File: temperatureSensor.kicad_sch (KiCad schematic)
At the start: 3 parts, among them J2 Conn_01x03_Pin

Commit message: revision
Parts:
- added TP1: TestPoint, TestPoint:TestPoint_THTPad_D2.0mm_Drill1.0mm, symbol Connector:TestPoint
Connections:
- net tempSensor1_OUT: now also TP1.1
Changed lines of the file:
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@@
     (effects (font (size 1.27 1.27)) (justify right))
+  )
+  (symbol (lib_id "Connector:TestPoint") (at 68.58 74.93 0) (unit 1)
+    (in_bom yes) (on_board yes) (dnp no) (fields_autoplaced)
+    (property "Reference" "TP1" (at 71.12 70.358 0)
+      (effects (font (size 1.27 1.27)) (justify left))
+    )
+    (property "Value" "TestPoint" (at 71.12 72.898 0)
+      (effects (font (size 1.27 1.27)) (justify left))
+    )
+    (property "Footprint" "TestPoint:TestPoint_THTPad_D2.0mm_Drill1.0mm" (at 73.66 74.93 0)
+      (effects (font (size 1.27 1.27)) hide)
+    )
+    (property "Datasheet" "~" (at 73.66 74.93 0)
+      (effects (font (size 1.27 1.27)) hide)
+    )
+    (pin "1")
+    (instances
+      (project "Telemetry-Peripheral-SOM-Daughterboard-IMU"
+        (path "/637f68f0-cb9c-412a-8573-5d8e7ef6d8a2/0366cb5e-31c7-40b1-9d0c-97ad688b48f0"
+          (reference "TP1") (unit 1)
+        )
+      )
+    )
   )
   (symbol (lib_id "Device:C") (at 110.49 97.79 0) (unit 1)

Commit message: Integrated changes made by BPS
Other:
- moved on the sheet: C7, C8, J2, TP1

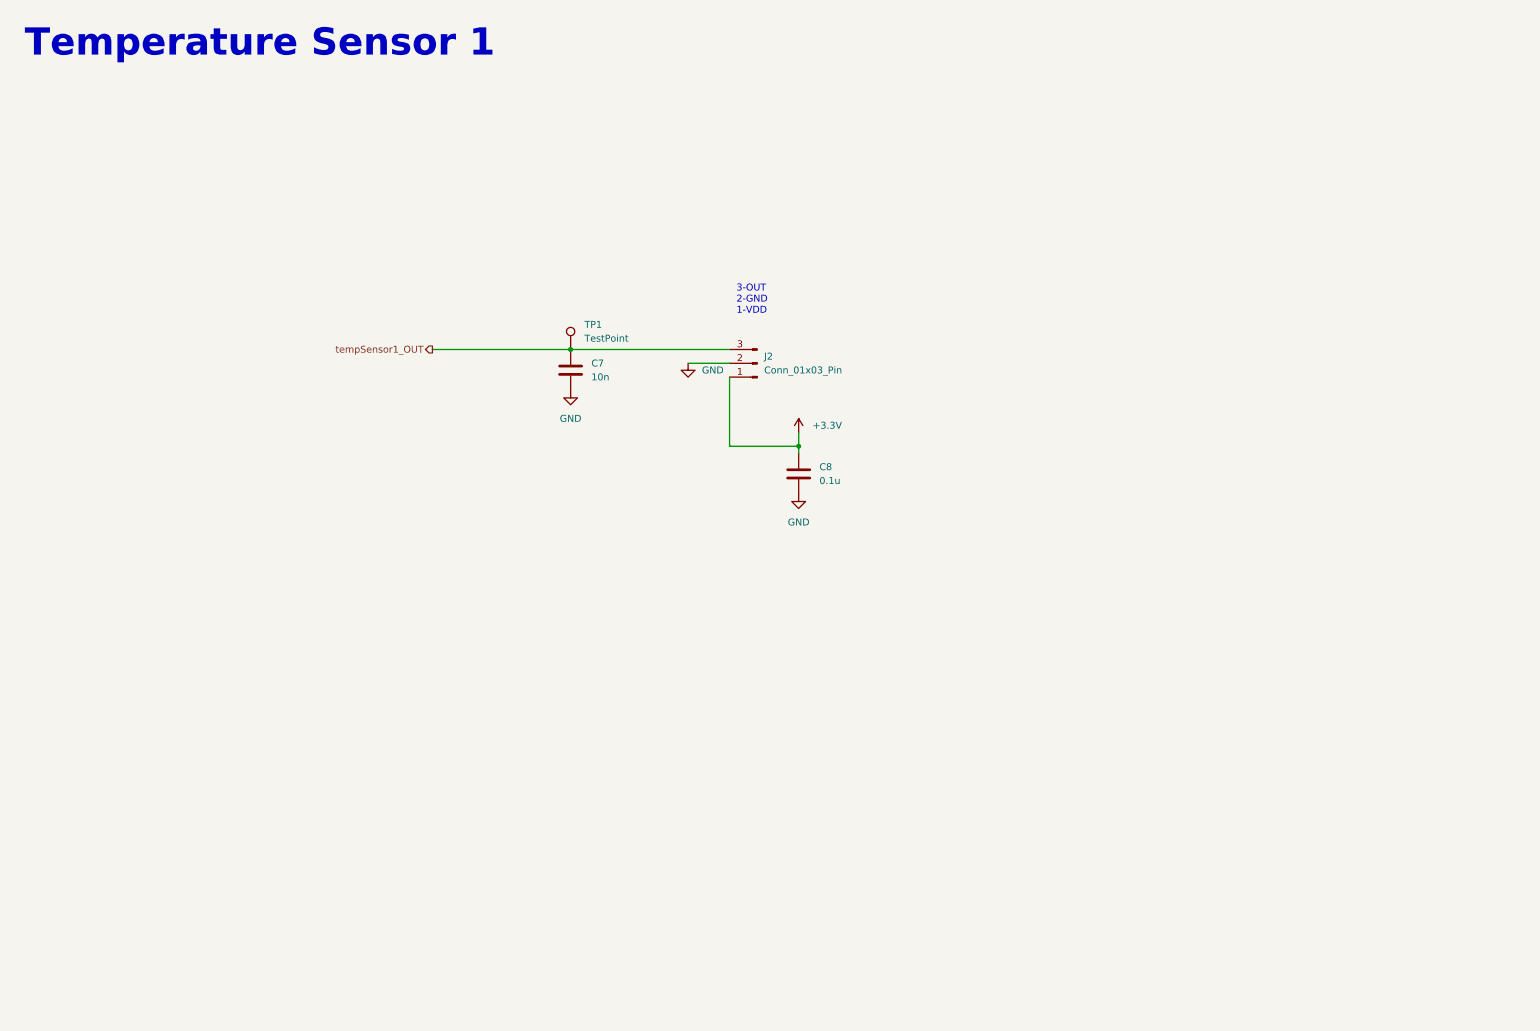
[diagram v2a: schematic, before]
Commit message: added protective circuitry for temp sensors, made name changes for IMU
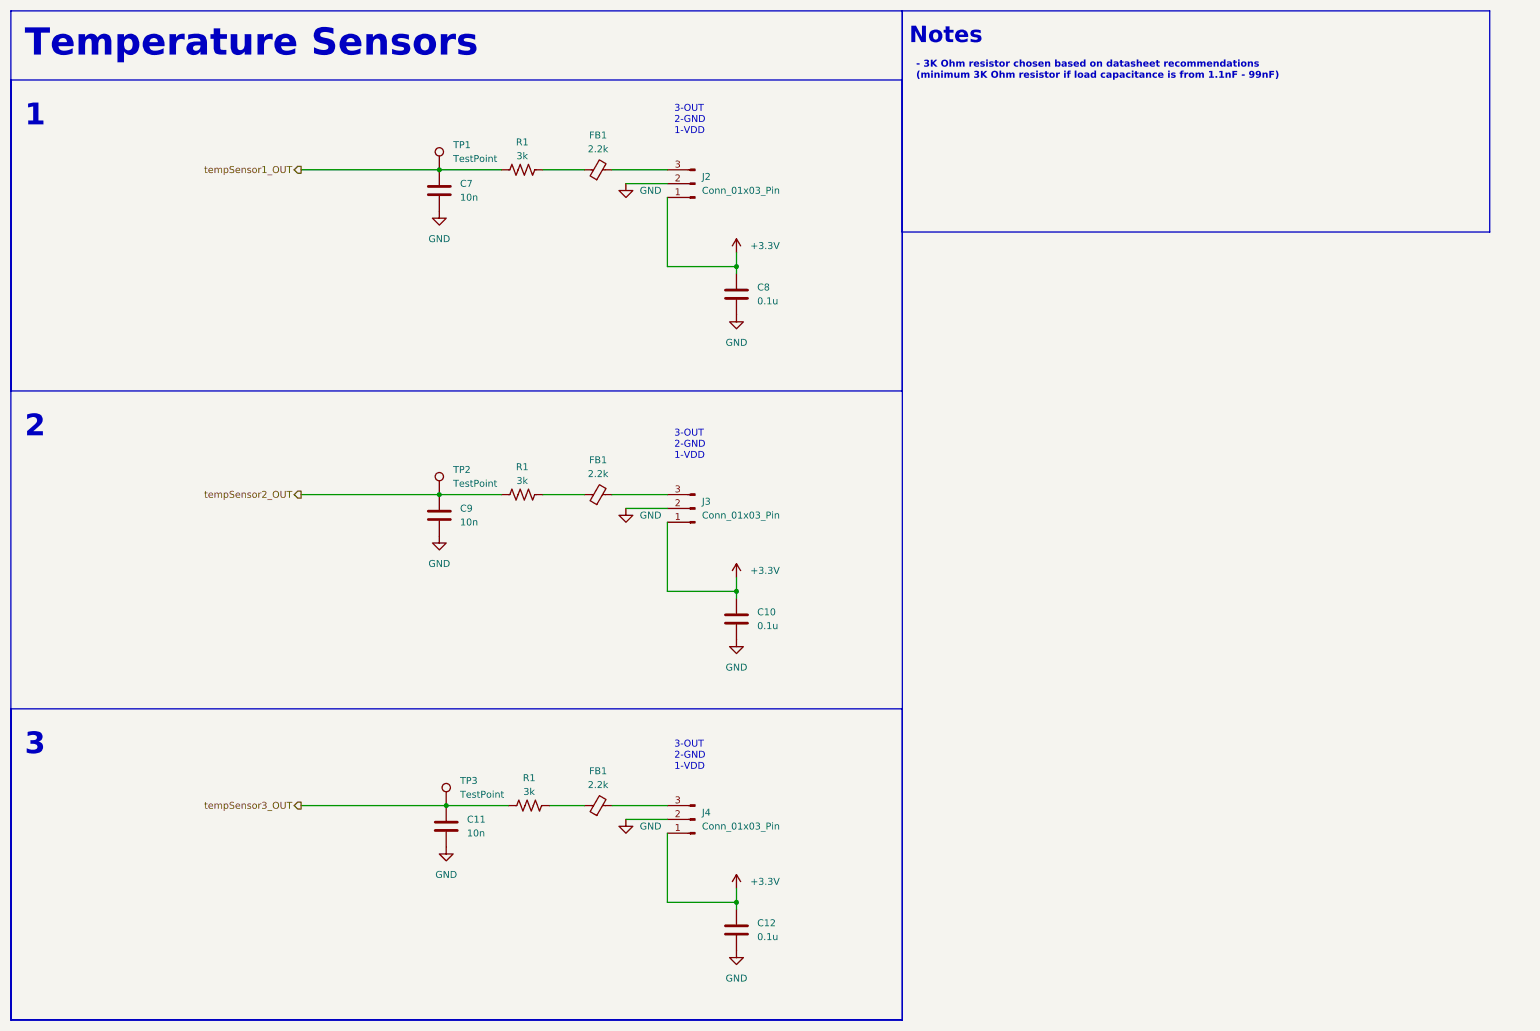
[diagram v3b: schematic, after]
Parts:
- added C10, C12: 0.1u, Capacitor_SMD:C_0805_2012Metric, symbol Device:C
- added C11, C9: 10n, Capacitor_SMD:C_0805_2012Metric, symbol Device:C
- added FB1 (x3): 2.2k, Inductor_SMD:L_0805_2012Metric_Pad1.05x1.20mm_HandSolder, symbol Device:FerriteBead_Small
- added J3, J4: Conn_01x03_Pin, UTSVT_Connectors:Molex_MicroFit3.0_1x3xP3.00mm_PolarizingPeg_Vertical, symbol Connector:Conn_01x03_Pin
- added R1 (x3): 3k, Resistor_SMD:R_0805_2012Metric_Pad1.20x1.40mm_HandSolder, symbol Device:R_US
- added TP2, TP3: TestPoint, TestPoint:TestPoint_THTPad_D2.0mm_Drill1.0mm, symbol Connector:TestPoint
- J2: Manufacturer_Name (none) -> Molex; Mouser Part Number (none) -> 538-43650-0315; P/N (none) -> 43650-0315
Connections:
- net +3.3V: now also C10.1, C12.1, J3.1 (Pin_1), J4.1 (Pin_1)
- net GND: now also C10.2, C11.2, C12.2, C9.2, J3.2 (Pin_2), J4.2 (Pin_2)
- net tempSensor1_OUT: now also R1.1; no longer J2.3 (Pin_3)
- new net: FB1.2, J4.3 (Pin_3)
- new net: FB1.2, J3.3 (Pin_3)
- new net: FB1.1, R1.2 (x3)
- new net: FB1.2, J2.3 (Pin_3)
- new net tempSensor2_OUT: C9.1, R1.1, TP2.1
- new net tempSensor3_OUT: C11.1, R1.1, TP3.1
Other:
- note added: "- 3K Ohm resistor chosen based on datasheet recommendations (minimum 3K Ohm resistor if load capacitance is from 1.1nF - 99nF)"
- note added: "1"
- note added: "2"
- note added: "3"
- note added: "Notes"
- note added: "Temperature Sensors"
- note removed: "Temperature Sensor 1"
- moved on the sheet: C7, C8, J2, TP1

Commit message: datasheet notes
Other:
- note added: "https://utexas.sharepoint.com/sites/ENGR-LonghornRacing/LHR%20Solar/Electrical /Data%20Acquisition/Datasheets/REN_FS3000_DST_20230207.pdf?CT=1698506826192&OR=ItemsView"
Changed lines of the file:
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@@
     (effects (font (size 4 4) (thickness 0.8) bold) (justify left bottom))
+  )
+  (text "https://utexas.sharepoint.com/sites/ENGR-LonghornRacing/LHR%20Solar/Electrical\n/Data%20Acquisition/Datasheets/REN_FS3000_DST_20230207.pdf?CT=1698506826192&OR=ItemsView\n"
+    (at 179.07 31.75 0)
+    (effects (font (size 1.27 1.27)) (justify left bottom))
   )
   (text "3" (at 15.24 149.86 0)

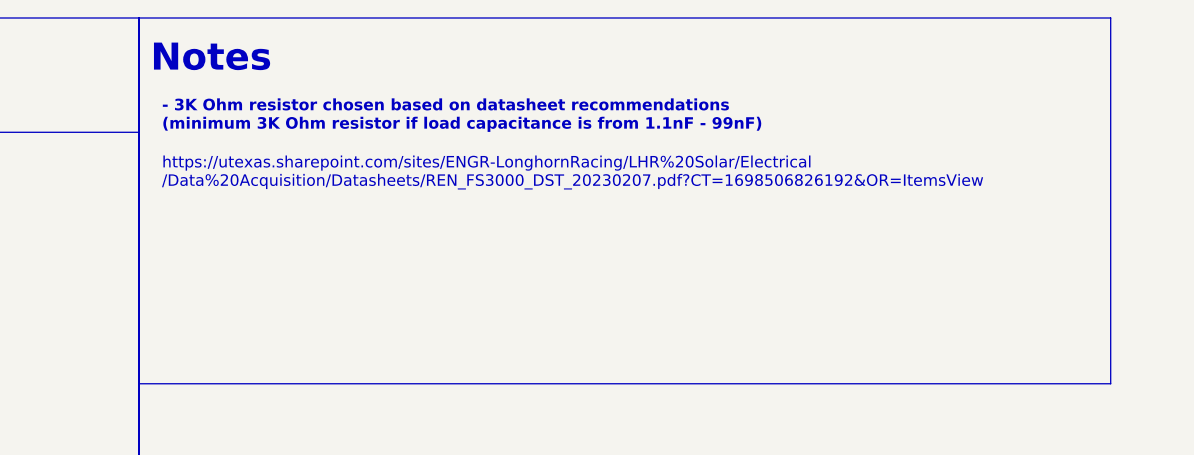
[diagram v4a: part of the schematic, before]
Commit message: Changes to routing and silkscreen, addressed schematic error
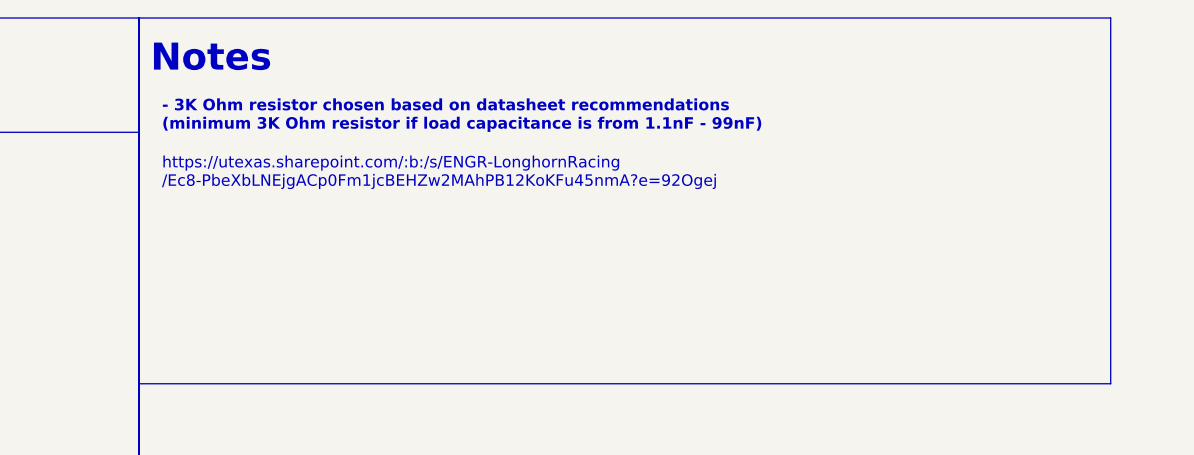
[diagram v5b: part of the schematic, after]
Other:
- note added: "https://utexas.sharepoint.com/:b:/s/ENGR-LonghornRacing /Ec8-PbeXbLNEjgACp0Fm1jcBEHZw2MAhPB12KoKFu45nmA?e=92Ogej"
- note removed: "https://utexas.sharepoint.com/sites/ENGR-LonghornRacing/LHR%20Solar/Electrical /Data%20Acquisition/Datasheets/REN_FS3000_DST_20230207.pdf?CT=1698506826192&OR=ItemsView"
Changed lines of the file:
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@@
     (effects (font (size 4 4) (thickness 0.8) bold) (justify left bottom))
   )
-  (text "https://utexas.sharepoint.com/sites/ENGR-LonghornRacing/LHR%20Solar/Electrical\n/Data%20Acquisition/Datasheets/REN_FS3000_DST_20230207.pdf?CT=1698506826192&OR=ItemsView\n"
+  (text "https://utexas.sharepoint.com/:b:/s/ENGR-LonghornRacing\n/Ec8-PbeXbLNEjgACp0Fm1jcBEHZw2MAhPB12KoKFu45nmA?e=92Ogej"
     (at 179.07 31.75 0)
     (effects (font (size 1.27 1.27)) (justify left bottom))
